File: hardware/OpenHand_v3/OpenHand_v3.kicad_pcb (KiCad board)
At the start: 4 copper layers, 100 x 50 mm, 191 parts, among them J1 CONN_MOTOR_1, J11 CONN_EMG_2, J12 CONN_SWD, J14 CONN_MOTOR_1_ENCODER, J15 CONN_MOTOR_2_ENCODER, J16 CONN_MOTOR_3_ENCODER, J2 CONN_MOTOR_2, J5 CONN_USB_C, J6 CONN_MOTOR_3, J7 CONN_FDBK, J8 CONN_EMG_1, SW1 BTN_RST, SW2 SW_Push, U1 STM32F103RETx, U10 DRV8833PWP, U3 AMS1117-3.3, U4 ICL7660, U5 TL084, U6 TL084, U7 DRV8833PWP, U8 DRV8833PWP, U9 DRV8833PWP, Y1 16MHz

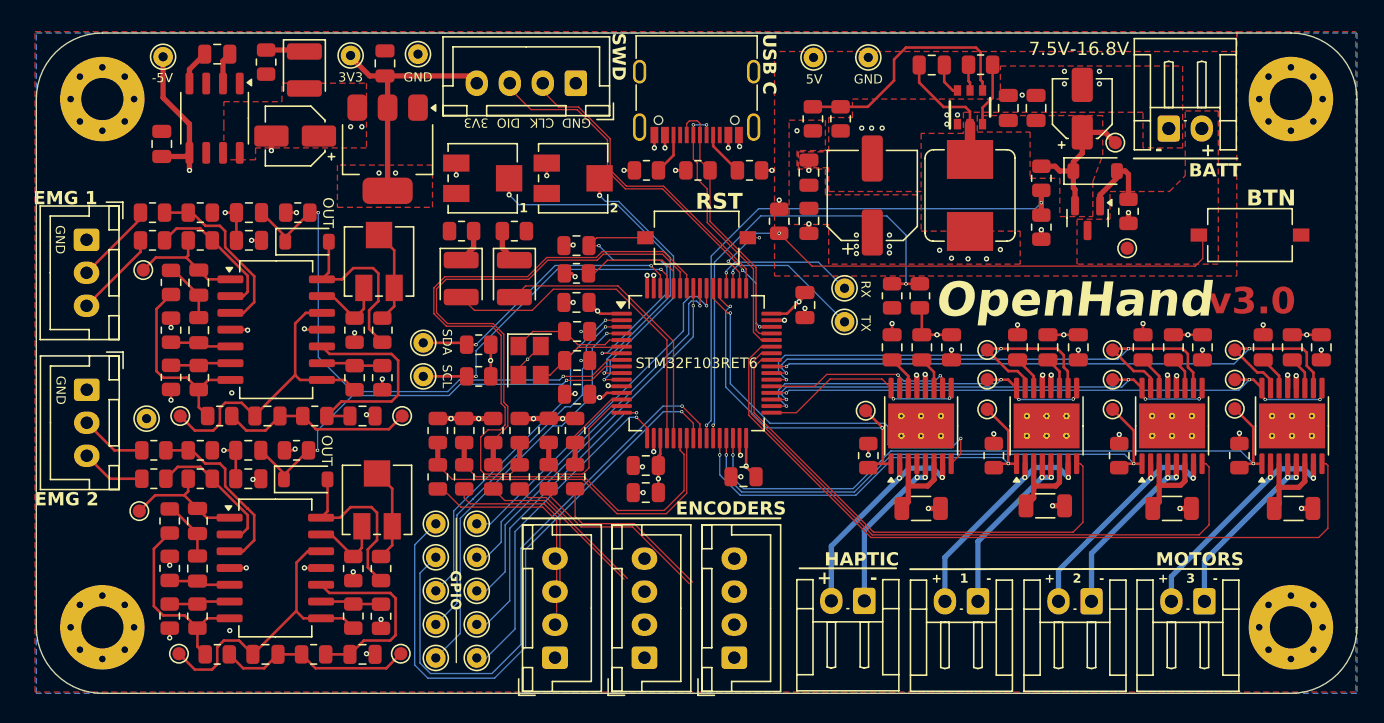
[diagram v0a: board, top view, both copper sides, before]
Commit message: Finalize board v3, prepare CubeIDE config
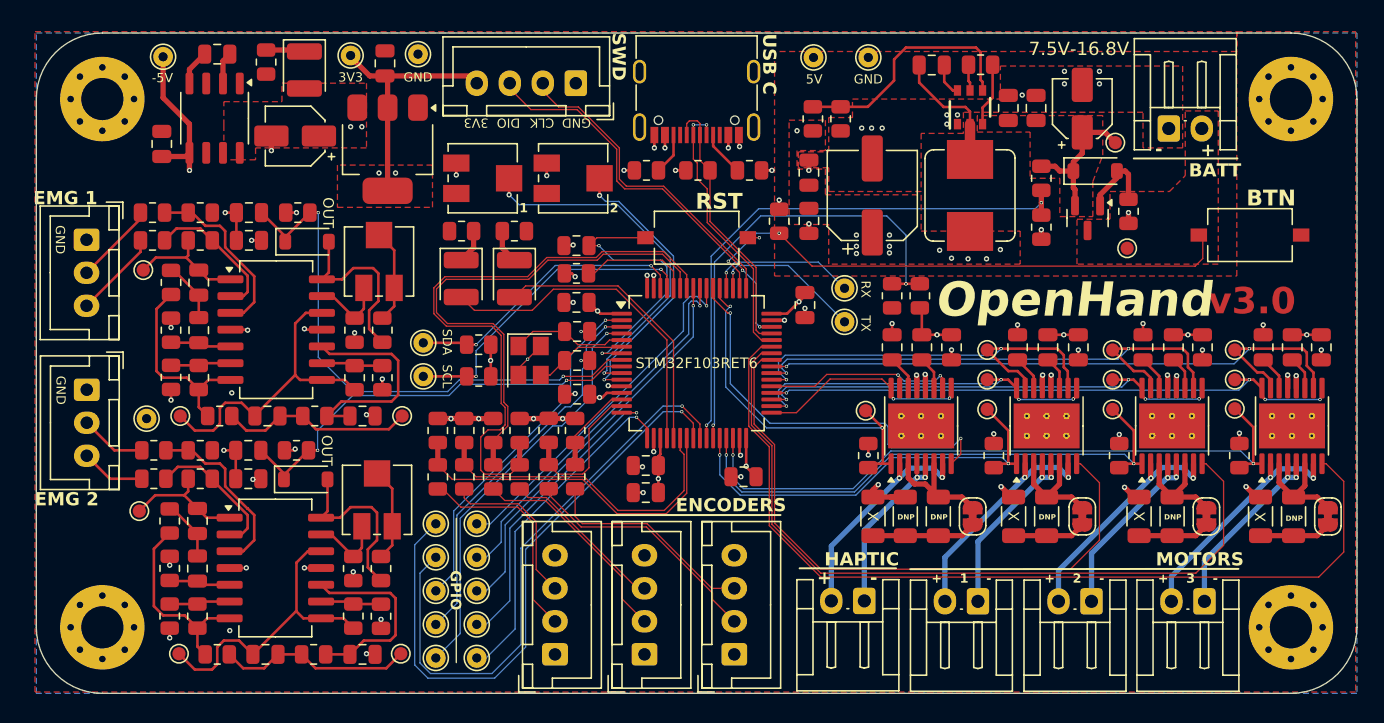
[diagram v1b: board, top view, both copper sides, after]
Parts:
- added JP1: JUMPER, Jumper:SolderJumper-2_P1.3mm_Bridged_RoundedPad1.0x1.5mm, F.Cu at (179.2, 136.6)
- added JP2: JUMPER, Jumper:SolderJumper-2_P1.3mm_Bridged_RoundedPad1.0x1.5mm, F.Cu at (188.6, 136.6)
- added JP3: JUMPER, Jumper:SolderJumper-2_P1.3mm_Bridged_RoundedPad1.0x1.5mm, F.Cu at (197.8, 136.6)
- added JP4: JUMPER, Jumper:SolderJumper-2_P1.3mm_Bridged_RoundedPad1.0x1.5mm, F.Cu at (170.9, 136.6)
- added R69: 0R2, Resistor_SMD:R_1206_3216Metric, F.Cu at (186.0, 136.6)
- added R70: 0R2, Resistor_SMD:R_1206_3216Metric, F.Cu at (176.5, 136.6)
- added R71: 0R2, Resistor_SMD:R_1206_3216Metric, F.Cu at (195.2, 136.6)
- added R72: 4R7, Resistor_SMD:R_1206_3216Metric, F.Cu at (165.8, 136.6)
- added R73: 4R7, Resistor_SMD:R_1206_3216Metric, F.Cu at (168.3, 136.6)
- C10, C11: value (none) -> 10u
- C12, C16: value (none) -> 1u
- C13: value (none) -> 100n
- C14: value (none) -> 47u
- C15: value (none) -> 22u
- D3: value (none) -> 5V Zener
- J3: value (none) -> CONN_BATT
- L1: value (none) -> 3.3uH
- Q1: value (none) -> AO3401A
- R10, R14: value (none) -> 47k
- R11, R12, R16: value (none) -> 10k
- R13: value (none) -> 54.9k
- TP15: value (none) -> TP_BATT_P
- TP16: value (none) -> TP_V_BATT
- U2: value (none) -> TPS565201DDCR
- moved R53 3.70 mm to (163.3, 136.6), turned to -90 degrees
- moved R48 2.57 mm to (183.5, 136.6), turned to -90 degrees
- moved R52 2.57 mm to (192.7, 136.6), turned to -90 degrees
- moved R47 2.53 mm to (174.0, 136.6), turned to -90 degrees
- moved J14 0.25 mm to (139.3, 147.1)
- moved J15 0.25 mm to (146.1, 147.1)
- moved J16 0.25 mm to (152.8, 147.1)
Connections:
- R47 pad 2: Net-(U7-AISEN) -> Net-(JP1-A)
- R48 pad 2: Net-(U8-AISEN) -> Net-(JP2-A)
- R52 pad 2: Net-(U9-AISEN) -> Net-(JP3-A)
- R53 pad 2: Net-(U10-AISEN) -> Net-(JP4-A)
- U10 pad 3: Net-(U10-AISEN) -> Net-(JP4-B)
- U10 pad 6: Net-(U10-AISEN) -> Net-(JP4-B)
- U7 pad 3: Net-(U7-AISEN) -> Net-(JP1-B)
- U7 pad 6: Net-(U7-AISEN) -> Net-(JP1-B)
- U8 pad 3: Net-(U8-AISEN) -> Net-(JP2-B)
- U8 pad 6: Net-(U8-AISEN) -> Net-(JP2-B)
- U9 pad 3: Net-(U9-AISEN) -> Net-(JP3-B)
- U9 pad 6: Net-(U9-AISEN) -> Net-(JP3-B)
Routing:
- net +5V: track 36.4 -> 50.8 mm
- net Net-(JP4-B): track 0.00 -> 9.54 mm
- net MOTOR_03_FAULT: track 59.6 -> 68.8 mm
- net Net-(JP1-B): track 0.00 -> 8.89 mm
- net MOTOR_01_FAULT: track 38.8 -> 47.6 mm
- net MOTOR_02_FAULT: track 49.5 -> 58.3 mm
- net Net-(JP3-B): track 0.00 -> 8.79 mm
- net Net-(JP2-B): track 0.00 -> 8.79 mm
- net Net-(JP4-A): track 0.00 -> 7.89 mm
- net Net-(U9-AISEN): track 7.01 -> 0.00 mm
- net Net-(U8-AISEN): track 6.99 -> 0.00 mm
- net Net-(U10-AISEN): track 6.95 -> 0.00 mm
- net Net-(U7-AISEN): track 6.91 -> 0.00 mm
- net Net-(JP1-A): track 0.00 -> 5.54 mm
- net Net-(JP3-A): track 0.00 -> 5.44 mm
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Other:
- board text added: "DNP"
- board text added: "X"

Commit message: Update PCB via size, start with code infrastructure idea
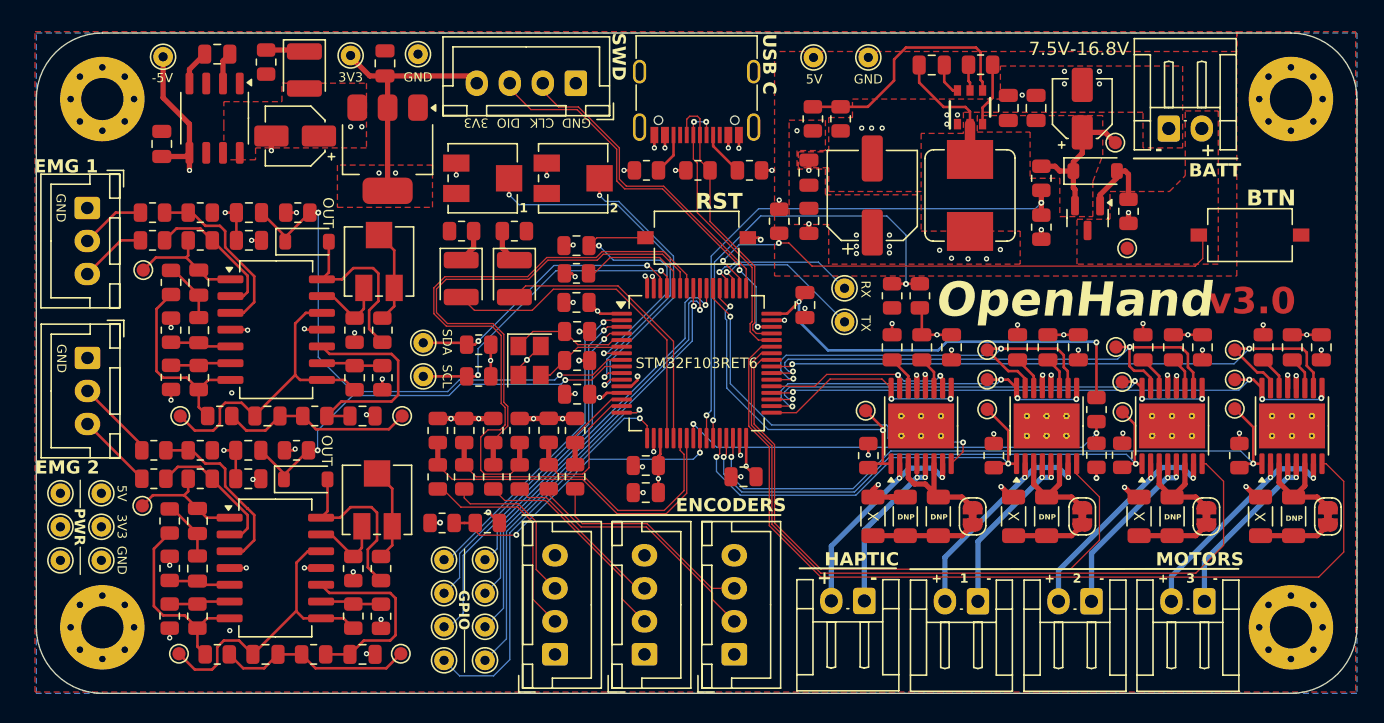
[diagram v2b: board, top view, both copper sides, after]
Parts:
- added R74: 10k, Resistor_SMD:R_0805_2012Metric, F.Cu at (180.3, 132.0)
- added R75: 10k, Resistor_SMD:R_0805_2012Metric, F.Cu at (134.2, 137.1)
- added TH1: 10k, Resistor_SMD:R_0805_2012Metric, F.Cu at (180.3, 128.5)
- added TH2: 10k, Resistor_SMD:R_0805_2012Metric, F.Cu at (130.7, 137.1)
- added TP10: TP_5V_1, TestPoint:TestPoint_THTPad_D1.5mm_Drill0.7mm, F.Cu at (101.8, 134.8)
- added TP11: TP_5V_2, TestPoint:TestPoint_THTPad_D1.5mm_Drill0.7mm, F.Cu at (104.9, 134.8)
- added TP9: TP_3V3_2, TestPoint:TestPoint_THTPad_D1.5mm_Drill0.7mm, F.Cu at (104.9, 137.4)
- TP1: value TP_UC_PC5 -> TP_GND_3
- TP5: value TP_UC_PC4 -> TP_GND_4
- TP6: value TP_GND_1 -> TP_3V3_1
- TP7: value TP_GND_2 -> TP_GND_1
- TP8: value TP_GND_3 -> TP_GND_2
- moved TP5 28.6 mm to (101.8, 139.9), turned to 0 degrees
- moved TP1 25.3 mm to (104.9, 139.9), turned to 0 degrees
- moved TP6 10.5 mm to (101.8, 137.4)
- moved TP37 2.79 mm to (134.0, 147.5)
- moved TP39 2.79 mm to (134.0, 139.9)
- moved TP40 2.79 mm to (134.0, 142.4)
- moved TP41 2.79 mm to (134.0, 145.0)
- moved TP38 2.48 mm to (130.9, 147.5)
- moved TP14 2.44 mm to (130.9, 142.4)
- moved TP4 2.44 mm to (130.9, 139.9)
- moved TP36 2.44 mm to (130.9, 145.0)
- moved J11 2.41 mm to (103.9, 124.6)
- moved J8 2.41 mm to (103.9, 113.2)
- moved TP27 0.78 mm to (182.2, 128.7)
- moved TP29 0.75 mm to (182.2, 126.4)
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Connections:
- TP1 pad 1: /PC5 -> GND
- TP5 pad 1: /PC4 -> GND
- TP6 pad 1: GND -> +3V3
- U1 pad 24: /PC4 -> PCB_TEMP_01
- U1 pad 25: /PC5 -> PCB_TEMP_02
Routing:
- net +3V3: track 42.9 -> 121.8 mm, vias 13 -> 15
- net /PC4: track 47.1 -> 0.00 mm, vias 1 -> 0
- net /PC5: track 44.3 -> 0.00 mm, vias 1 -> 0
- net PCB_TEMP_01: track 0.00 -> 34.4 mm, vias 0 -> 2
- net PCB_TEMP_02: track 0.00 -> 23.1 mm, vias 0 -> 2
- net /PA3: track 25.2 -> 30.7 mm
- net /PB4: track 28.0 -> 31.4 mm
- net /PA2: track 22.4 -> 25.8 mm
- net GND: track 66.3 -> 69.4 mm, vias 73 -> 75
- net /PC14: track 29.3 -> 26.4 mm
- net /PC15: track 31.5 -> 28.6 mm
- net /PB5: track 29.4 -> 32.2 mm
- net /PC13: track 27.0 -> 24.6 mm
- net /PB3: track 26.7 -> 29.0 mm
- net EMG_01_N: track 6.65 -> 5.09 mm
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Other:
- board text added: "A2"
- board text added: "A3"
- board text added: "B3"
- board text added: "B4"
- board text added: "B5"
- board text added: "C13"
- board text added: "C14"
- board text added: "C15"
- board text added: "PWR"
- board text removed: "PA2"
- board text removed: "PA3"
- board text removed: "PB3"
- board text removed: "PB4"
- board text removed: "PB5"
- board text removed: "PC13"
- board text removed: "PC14"
- board text removed: "PC15"
- board text removed: "PC4"
- board text removed: "PC5"

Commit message: Update PCB with larger vias, add board temp sensor
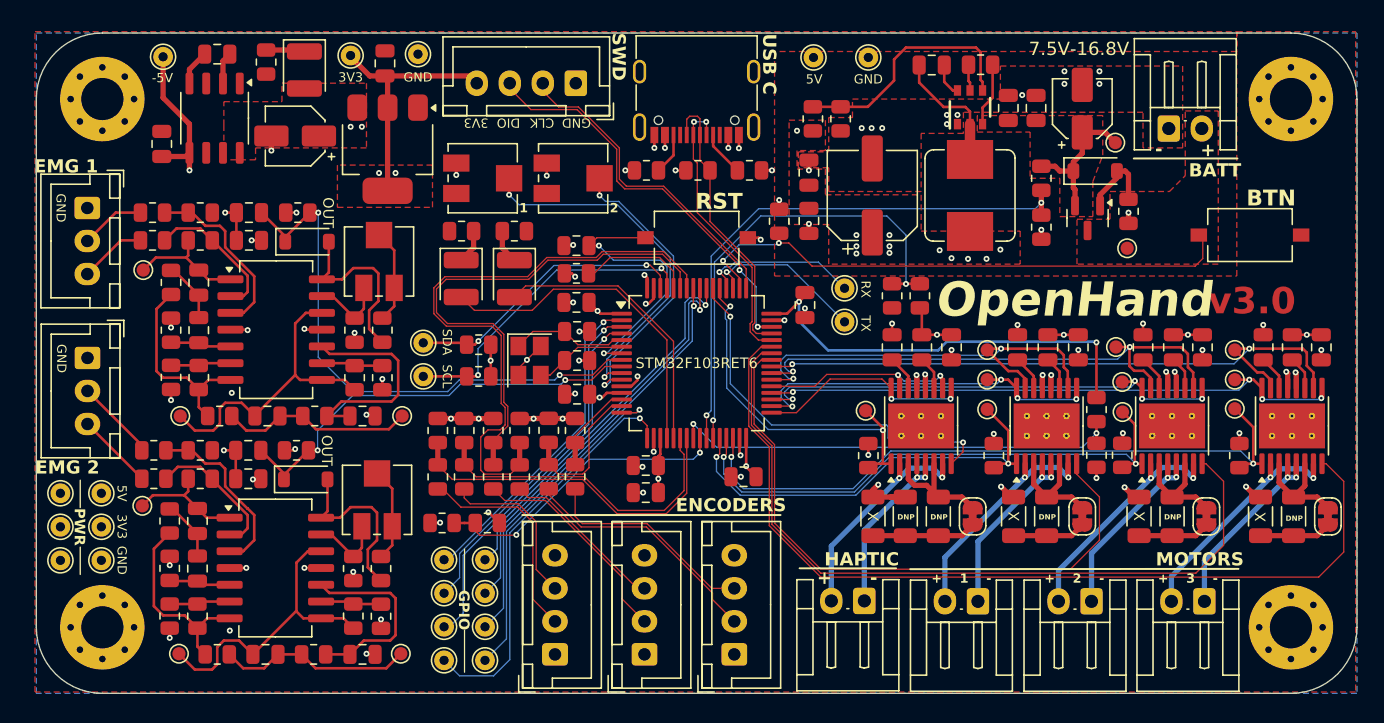
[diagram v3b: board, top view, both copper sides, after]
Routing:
- net GND: track 69.4 -> 70.4 mm
- net +5V: track 50.9 -> 51.5 mm
